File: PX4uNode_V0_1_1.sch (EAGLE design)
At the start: 130 parts, among them M3_MOUNT1101 MOUNT-HOLE3.1MM, M3_MOUNT1102 MOUNT-HOLE3.1MM, M3_MOUNT1103 MOUNT-HOLE3.1MM, M3_MOUNT1104 MOUNT-HOLE3.1MM, U101 STM32F4X7VX, U401 MAX3051, U402 MAX3051, X101 3.2x2.5 mm / 24 MHz / 15 ppm

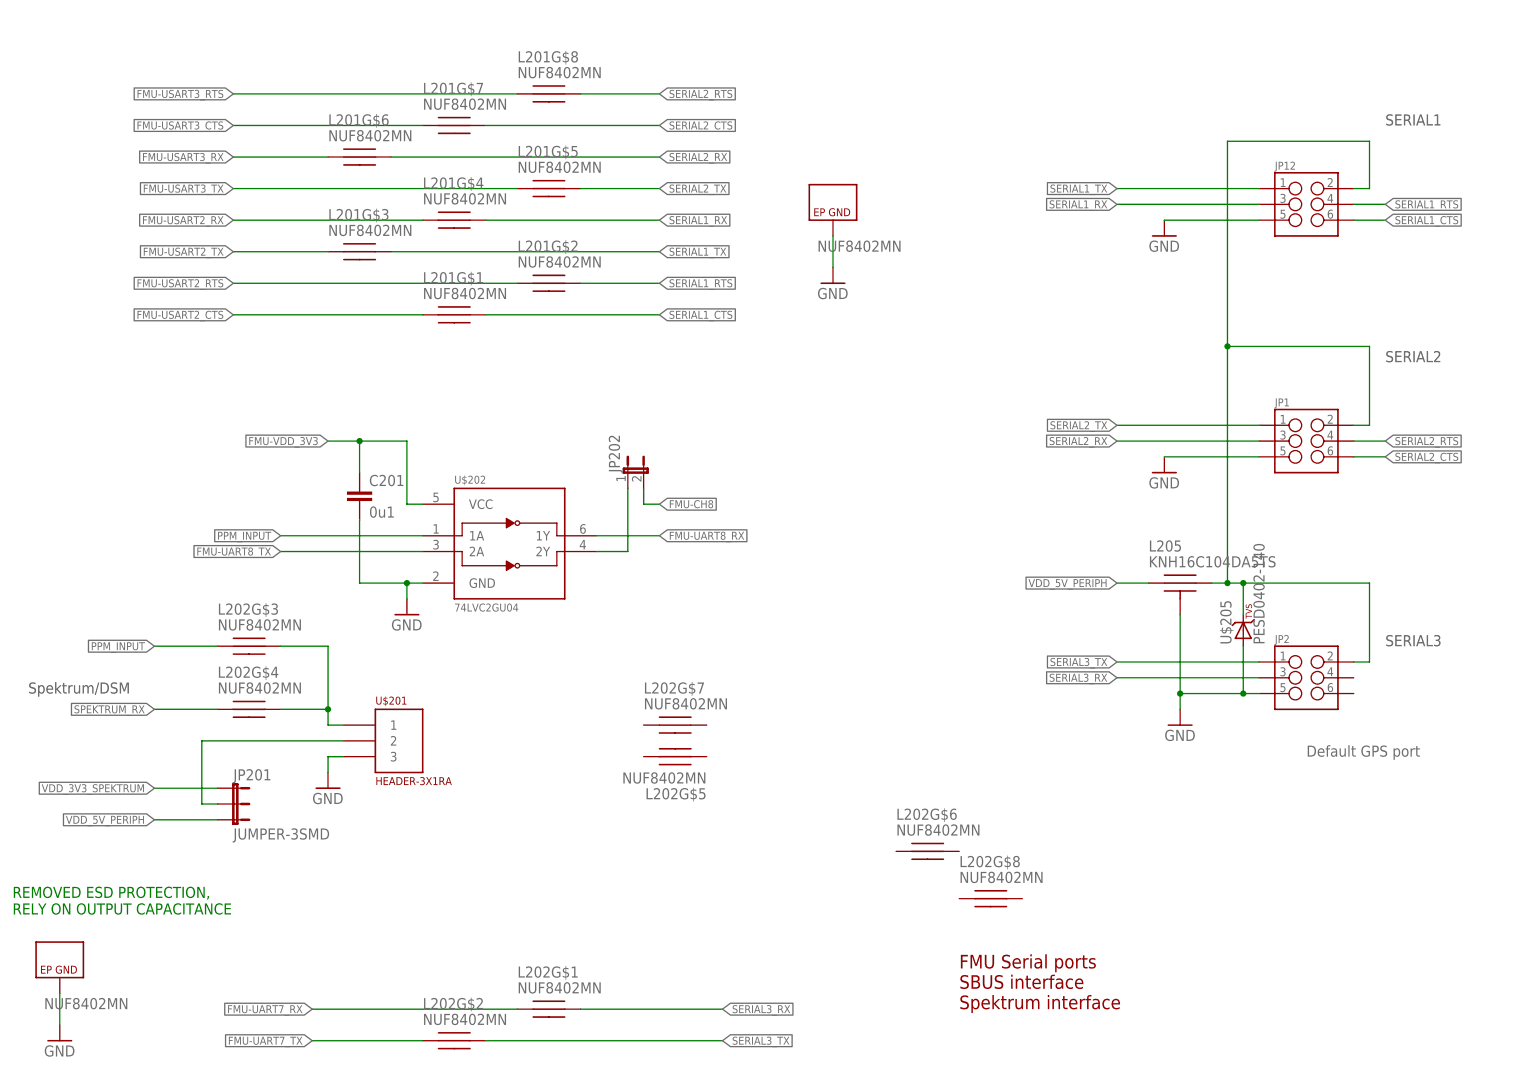
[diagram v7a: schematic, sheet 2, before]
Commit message: UART 3 ESD swap
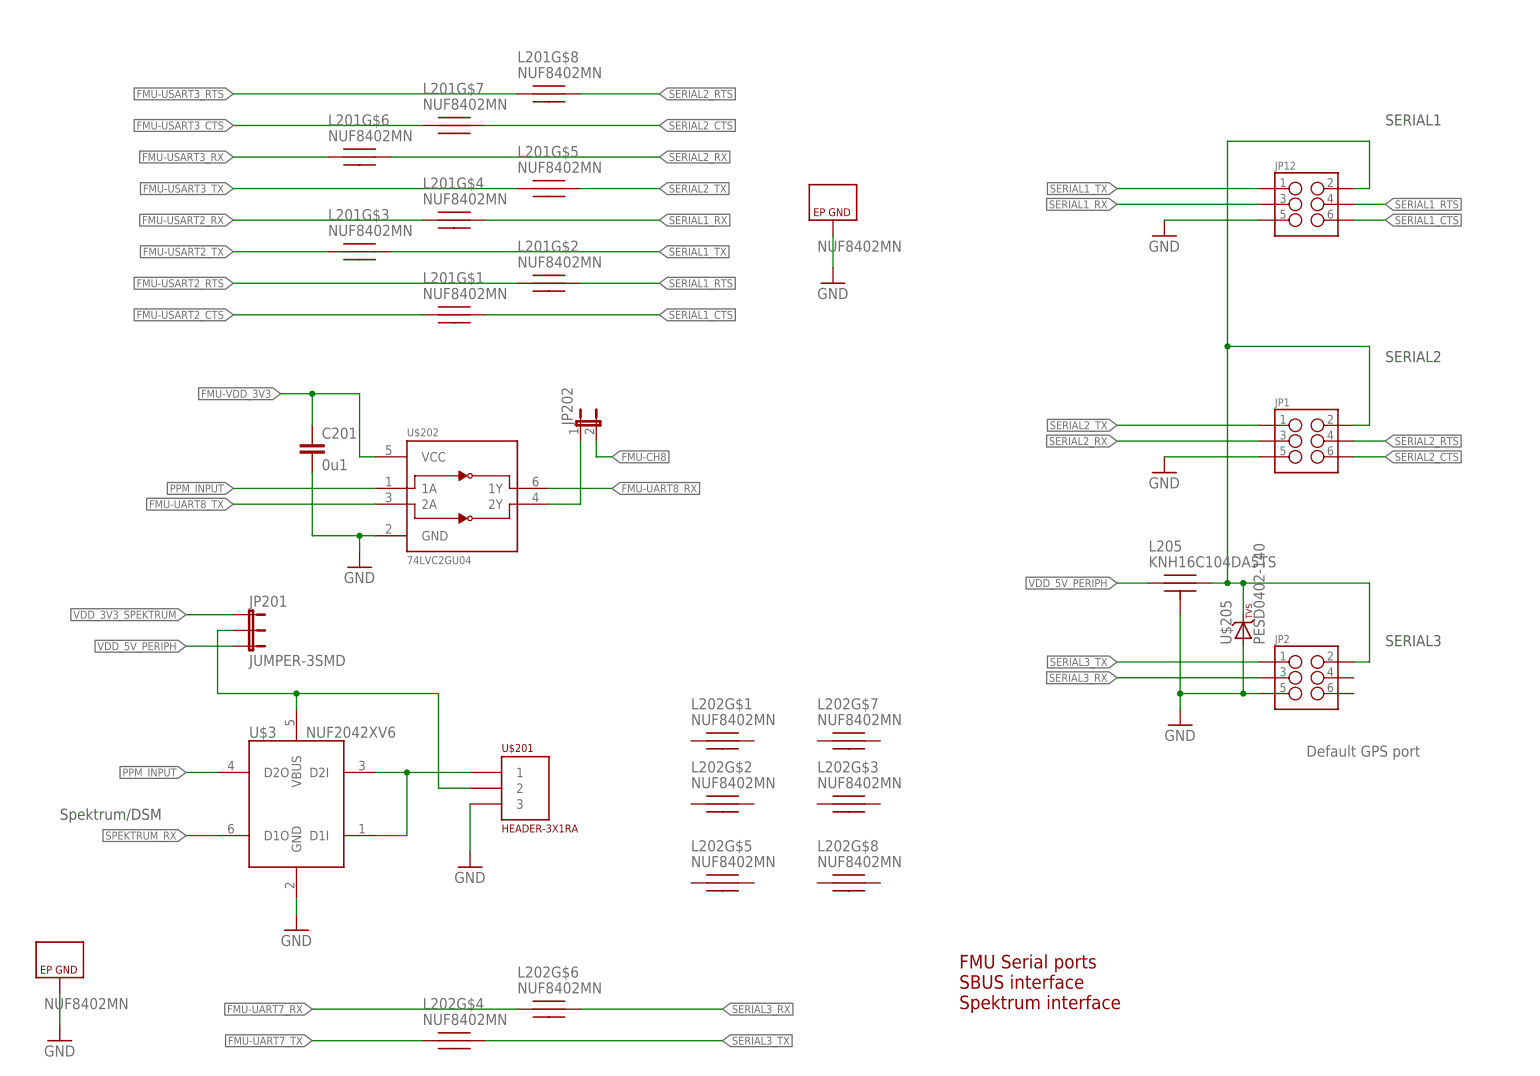
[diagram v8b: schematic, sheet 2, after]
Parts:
- added U$3: NUF2042XV6, PX4lite:NUF2042XV6
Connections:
- removed net VDD_RX_POWER: JP201.2, U$201.2
- new net N$2: U$201.1, U$3.D1I, U$3.D2I
- net FMU-UART7_RX: now also L202G$6.P$1; no longer L202G$1.P$1
- net FMU-UART7_TX: now also L202G$4.P$1; no longer L202G$2.P$1
- net GND: now also U$3.GND
- net N$18: now also JP201.2, U$201.2, U$3.VBUS; no longer L202G$3.P$2, L202G$4.P$2, U$201.1
- net PPM_INPUT: now also U$3.D2O; no longer L202G$3.P$1
- net SERIAL3_RX: now also L202G$6.P$2; no longer L202G$1.P$2
- net SERIAL3_TX: now also L202G$4.P$2; no longer L202G$2.P$2
- net SPEKTRUM_RX: now also U$3.D1O; no longer L202G$4.P$1
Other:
- note removed: "REMOVED ESD PROTECTION, RELY ON OUTPUT CAPACITANCE"
- moved on the sheet: C201, JP201, JP202, L202G$1, L202G$2, L202G$3, L202G$4, L202G$5, L202G$6, L202G$7, L202G$8, U$201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
